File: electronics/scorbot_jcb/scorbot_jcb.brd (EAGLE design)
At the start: 64.4 x 84.6 mm, 13 parts

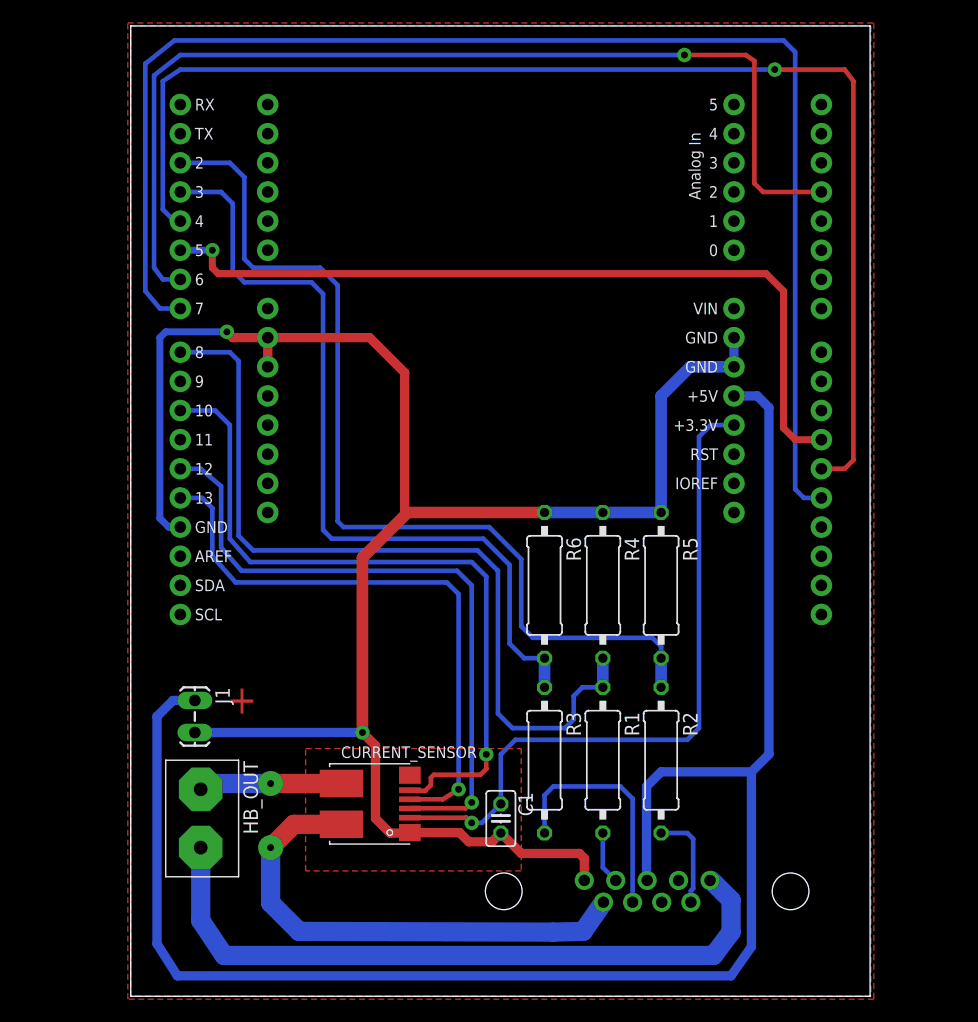
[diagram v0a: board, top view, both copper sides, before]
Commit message: Fix board orientation
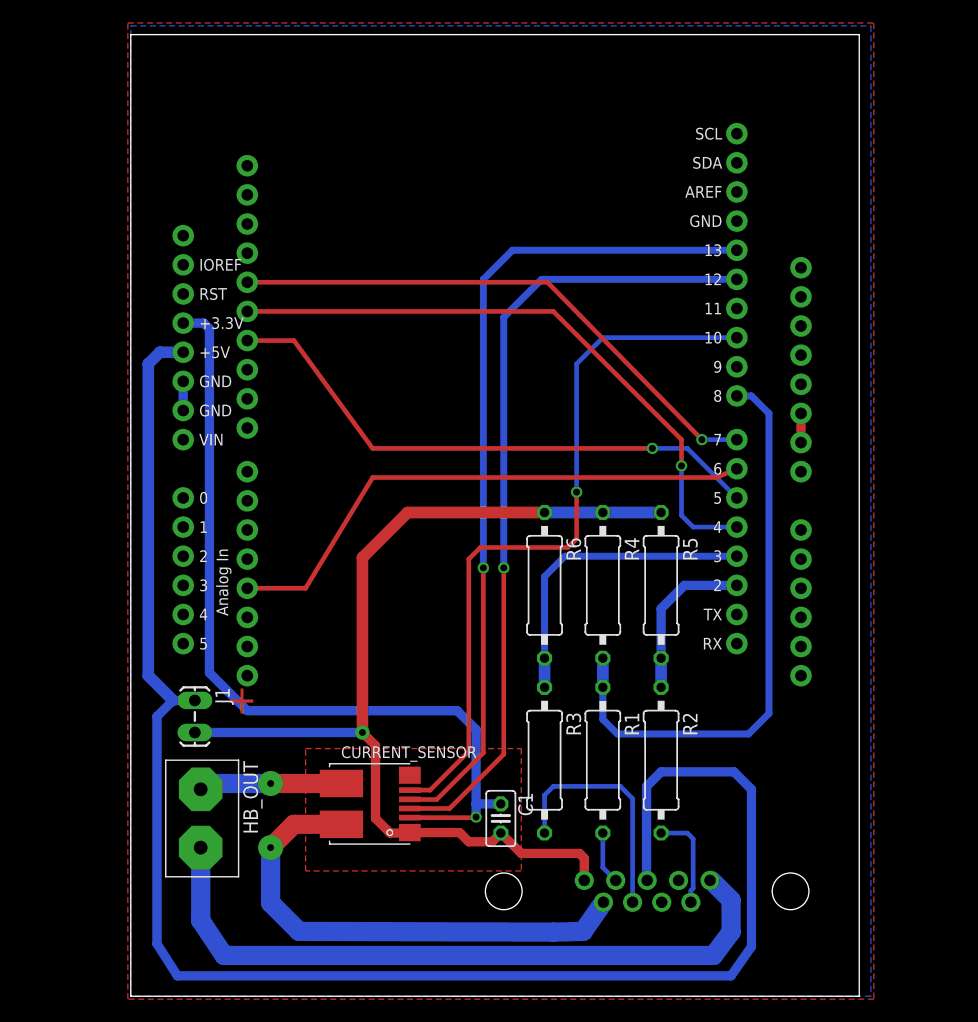
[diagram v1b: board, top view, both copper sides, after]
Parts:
- moved XMC4800 82.1 mm to (55.4, 85.3), turned to 180 degrees
- moved HBRIDGE 81.1 mm to (7.62, 82.5), turned to 180 degrees
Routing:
- net INH2: track 122.1 -> 48.4 mm, vias 0 -> 1
- net GND: track 164.0 -> 93.3 mm, vias 2 -> 1
- net ENC_A: track 82.6 -> 14.3 mm
- net INH1: track 110.3 -> 54.3 mm
- net ENC_B: track 70.6 -> 27.2 mm
- net IN1: track 89.5 -> 48.3 mm, vias 1 -> 0
- net IN2: track 70.6 -> 49.2 mm
- net HOME: track 71.8 -> 50.7 mm
- net SCLK: track 51.8 -> 72.5 mm
- net +3V3: track 60.2 -> 73.3 mm
- net MISO: track 57.3 -> 69.9 mm
- net +5V: track 147.3 -> 144.3 mm
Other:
- board size 64.4 x 84.6 mm -> 63.5 x 83.8 mm

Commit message: Holes and via correction
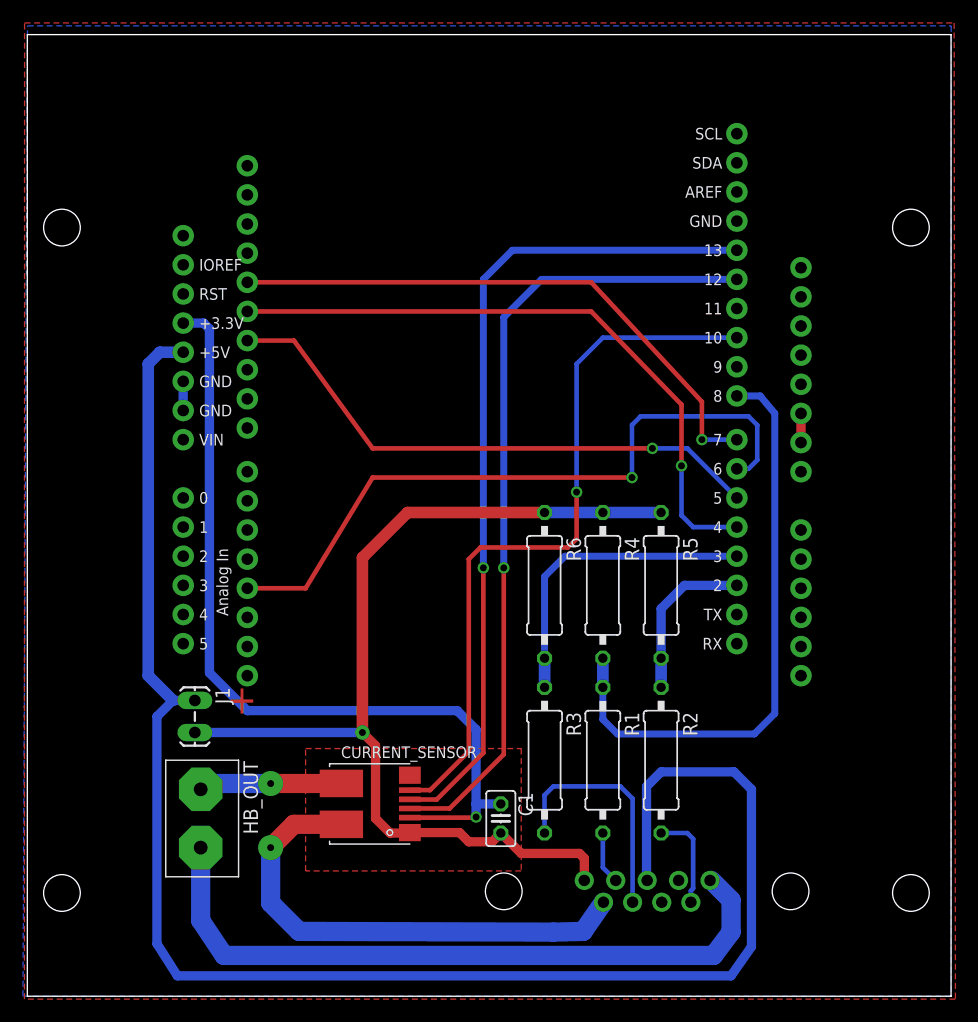
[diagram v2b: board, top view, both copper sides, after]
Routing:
- net IN1: track 48.3 -> 60.2 mm, vias 0 -> 1
- net INH2: track 48.4 -> 50.5 mm
- net INH1: track 54.3 -> 56.2 mm
- net HOME: track 50.7 -> 51.8 mm
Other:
- board size 63.5 x 83.8 mm -> 80.5 x 83.8 mm
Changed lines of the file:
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@@
 <?xml version="1.0" encoding="utf-8"?>
 <!DOCTYPE eagle SYSTEM "eagle.dtd">
-<eagle version="7.4.0">
+<eagle version="7.5.0">
 <drawing>
 <settings>
@@
 <setting verticaltext="up"/>
 </settings>
-<grid distance="0.01" unitdist="inch" unit="inch" style="lines" multiple="1" display="yes" altdistance="0.025" altunitdist="inch" altunit="inch"/>
+<grid distance="100" unitdist="mil" unit="mil" style="lines" multiple="1" display="yes" altdistance="0.025" altunitdist="inch" altunit="inch"/>
 <layers>
 <layer number="1" name="Top" color="4" fill="1" visible="yes" active="yes"/>
@@
 <layer number="43" name="vRestrict" color="2" fill="10" visible="yes" active="yes"/>
 <layer number="44" name="Drills" color="7" fill="1" visible="no" active="yes"/>
-<layer number="45" name="Holes" color="7" fill="1" visible="no" active="yes"/>
+<layer number="45" name="Holes" color="7" fill="1" visible="yes" active="yes"/>
 <layer number="46" name="Milling" color="3" fill="1" visible="no" active="yes"/>
 <layer number="47" name="Measures" color="7" fill="1" visible="no" active="yes"/>
@@
 <board>
 <plain>
-<wire x1="0" y1="0" x2="63.5" y2="0" width="0" layer="20"/>
-<wire x1="63.5" y1="0" x2="63.5" y2="83.82" width="0" layer="20"/>
-<wire x1="63.5" y1="83.82" x2="0" y2="83.82" width="0" layer="20"/>
-<wire x1="0" y1="83.82" x2="0" y2="0" width="0" layer="20"/>
+<wire x1="-9.017" y1="0" x2="71.501" y2="0" width="0" layer="20"/>
+<wire x1="71.501" y1="0" x2="71.501" y2="83.82" width="0" layer="20"/>
+<wire x1="71.501" y1="83.82" x2="-9.017" y2="83.82" width="0" layer="20"/>
+<wire x1="-9.017" y1="83.82" x2="-9.017" y2="0" width="0" layer="20"/>
 <text x="8.382" y="24.638" size="2.54" layer="1" ratio="20">+</text>
+<hole x="-6" y="67" drill="3.2"/>
+<hole x="-6" y="9" drill="3.2"/>
+<hole x="68" y="9" drill="3.2"/>
+<hole x="68" y="67" drill="3.2"/>
 </plain>
 <attributes>
@@
 <wire x1="34.036" y1="12.446" x2="32.258" y2="14.224" width="0.8128" layer="1"/>
 <polygon width="0.4064" layer="16" isolate="1.016">
-<vertex x="0" y="0"/>
-<vertex x="0" y="84.582"/>
-<vertex x="64.516" y="84.582"/>
-<vertex x="64.516" y="0"/>
+<vertex x="-9.398" y="0"/>
+<vertex x="-9" y="84.582"/>
+<vertex x="71.516" y="84.582"/>
+<vertex x="71.501" y="0"/>
 </polygon>
 <polygon width="0.4064" layer="1" isolate="1.016">
-<vertex x="-0.254" y="-0.254"/>
-<vertex x="-0.254" y="84.836"/>
-<vertex x="64.77" y="84.836"/>
-<vertex x="64.77" y="-0.254"/>
+<vertex x="-9.271" y="-0.254"/>
+<vertex x="-9.254" y="84.836"/>
+<vertex x="71.77" y="84.836"/>
+<vertex x="71.882" y="-0.254"/>
 </polygon>
 </signal>
@@
 <wire x1="10.16" y1="35.56" x2="15.24" y2="35.56" width="0.4064" layer="1"/>
 <wire x1="15.24" y1="35.56" x2="21.082" y2="45.212" width="0.4064" layer="1"/>
-<wire x1="21.082" y1="45.212" x2="51.054" y2="45.212" width="0.4064" layer="1"/>
-<wire x1="51.054" y1="45.212" x2="52.832" y2="45.974" width="0.4064" layer="1"/>
+<wire x1="52.832" y1="45.974" x2="53.848" y2="45.974" width="0.4064" layer="16"/>
+<wire x1="53.848" y1="45.974" x2="54.61" y2="46.736" width="0.4064" layer="16"/>
+<wire x1="54.61" y1="46.736" x2="54.61" y2="49.784" width="0.4064" layer="16"/>
+<wire x1="54.61" y1="49.784" x2="53.848" y2="50.546" width="0.4064" layer="16"/>
+<wire x1="53.848" y1="50.546" x2="44.45" y2="50.546" width="0.4064" layer="16"/>
+<wire x1="44.45" y1="50.546" x2="43.688" y2="49.784" width="0.4064" layer="16"/>
+<wire x1="43.688" y1="49.784" x2="43.688" y2="45.212" width="0.4064" layer="16"/>
+<via x="43.688" y="45.212" extent="1-16" drill="0.6" shape="square"/>
+<wire x1="43.688" y1="45.212" x2="21.082" y2="45.212" width="0.4064" layer="1"/>
 </signal>
 <signal name="IN2">
@@
 <wire x1="48.006" y1="41.91" x2="48.006" y2="46.228" width="0.4064" layer="16"/>
 <via x="48.006" y="46.228" extent="1-16" drill="0.6" shape="square"/>
-<wire x1="48.006" y1="46.228" x2="48.006" y2="48.514" width="0.4064" layer="1"/>
-<wire x1="48.006" y1="48.514" x2="36.83" y2="59.69" width="0.4064" layer="1"/>
-<wire x1="36.83" y1="59.69" x2="10.16" y2="59.69" width="0.4064" layer="1"/>
+<wire x1="48.006" y1="46.228" x2="48.006" y2="51.562" width="0.4064" layer="1"/>
+<wire x1="48.006" y1="51.562" x2="40.132" y2="59.69" width="0.4064" layer="1"/>
+<wire x1="40.132" y1="59.69" x2="10.16" y2="59.69" width="0.4064" layer="1"/>
 </signal>
 <signal name="INH2">
 <contactref element="XMC4800" pad="D7"/>
 <contactref element="HBRIDGE" pad="D13"/>
-<wire x1="10.16" y1="62.23" x2="36.322" y2="62.23" width="0.4064" layer="1"/>
-<wire x1="36.322" y1="62.23" x2="49.784" y2="48.514" width="0.4064" layer="1"/>
+<wire x1="10.16" y1="62.23" x2="40.132" y2="62.23" width="0.4064" layer="1"/>
+<wire x1="40.132" y1="62.23" x2="49.784" y2="51.816" width="0.4064" layer="1"/>
+<wire x1="49.784" y1="51.816" x2="49.784" y2="48.514" width="0.4064" layer="1"/>
 <via x="49.784" y="48.514" extent="1-16" drill="0.6" shape="square"/>
 <wire x1="49.784" y1="48.514" x2="52.832" y2="48.514" width="0.4064" layer="16"/>
@@
 <contactref element="R1" pad="1"/>
 <wire x1="41.148" y1="26.924" x2="41.148" y2="29.464" width="1.016" layer="16"/>
-<wire x1="52.832" y1="52.324" x2="54.102" y2="52.324" width="0.6096" layer="16"/>
-<wire x1="54.102" y1="52.324" x2="55.626" y2="50.8" width="0.6096" layer="16"/>
-<wire x1="55.626" y1="50.8" x2="55.626" y2="24.638" width="0.6096" layer="16"/>
-<wire x1="55.626" y1="24.638" x2="53.848" y2="22.86" width="0.6096" layer="16"/>
-<wire x1="53.848" y1="22.86" x2="42.418" y2="22.86" width="0.6096" layer="16"/>
+<wire x1="52.832" y1="52.324" x2="54.864" y2="52.324" width="0.6096" layer="16"/>
+<wire x1="54.864" y1="52.324" x2="56.134" y2="50.8" width="0.6096" layer="16"/>
+<wire x1="56.134" y1="50.8" x2="56.134" y2="24.638" width="0.6096" layer="16"/>
+<wire x1="56.134" y1="24.638" x2="54.356" y2="22.86" width="0.6096" layer="16"/>
+<wire x1="54.356" y1="22.86" x2="42.418" y2="22.86" width="0.6096" layer="16"/>
 <wire x1="42.418" y1="22.86" x2="41.148" y2="24.13" width="0.6096" layer="16"/>
 <wire x1="41.148" y1="24.13" x2="41.148" y2="26.924" width="0.6096" layer="16"/>
